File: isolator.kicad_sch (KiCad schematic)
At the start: 6 parts, among them U1 ADuM4165, U2 NUP4202, U3 NUP4202, Y1 24M

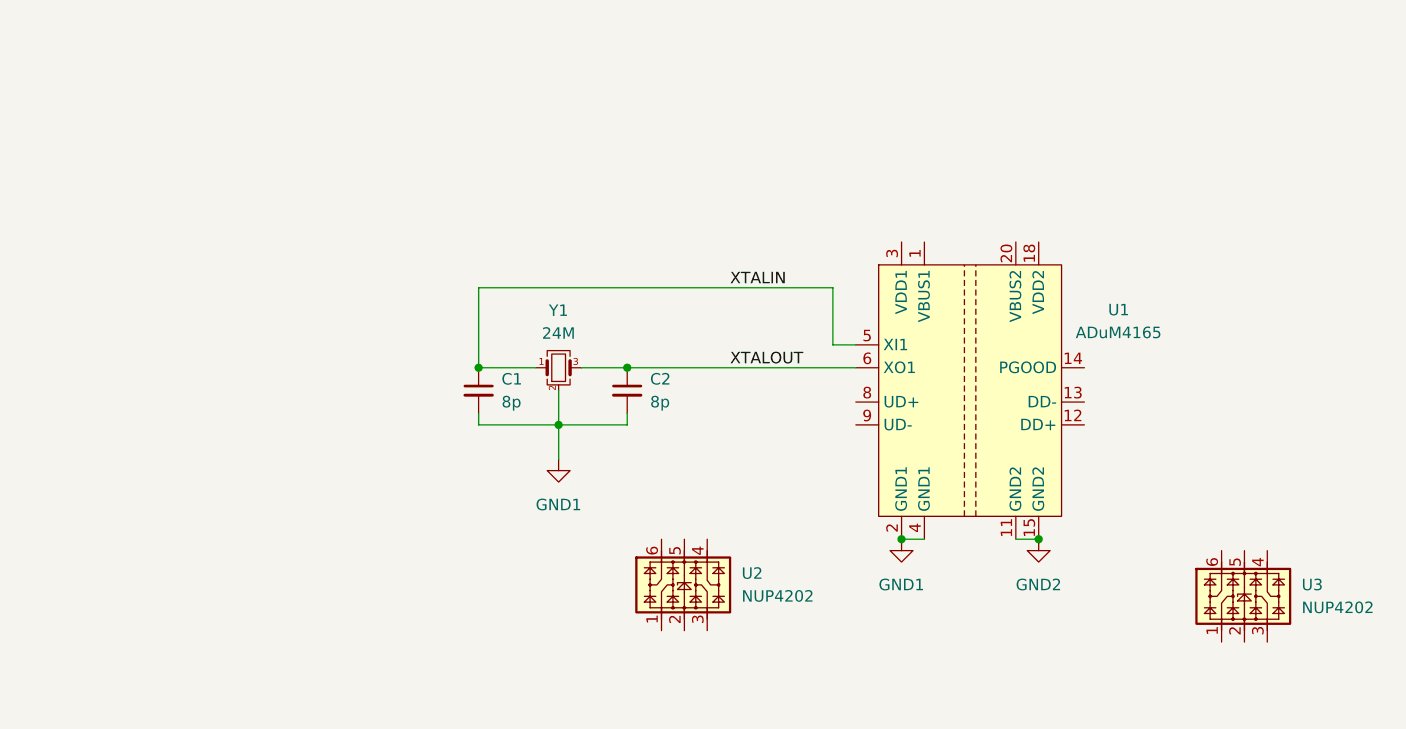
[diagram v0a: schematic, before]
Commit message: feat(sch): upstream USB-C host section
Add J1 (USB-C receptacle), R1/R2 (CC pull-downs), C3-C5 (VBUS_HOST/VDD1
decoupling) and wire VBUS_HOST, HOST_DP, HOST_DM, GND1 per the task-4
brief. Rewire U2 (NUP4202) as the host-side ESD array: two of its four
I/O channels clamp HOST_DP/HOST_DM, its GND pin ties to GND1, its VBUS
pin ties to VBUS_HOST, and the two unused channels get no_connect.
Terminate all ADuM4165 (U1) Side-1 pins; Side-2 pins not yet used by
this task get explicit no_connect markers.

Also add PWR_FLAG symbols on GND1, GND2, VBUS_HOST and VDD1, and
no_connect markers on U3's six pins, so `kicad-cli sch erc` exits 0
across the whole file (the project's ERC config marks
power_pin_not_driven as an error, and U3/GND2 were already unwired
pre-existing state) — flagged in the task report for whoever wires
U3/GND2 downstream.

Co-Authored-By: Claude Fable 5 <noreply@anthropic.com>
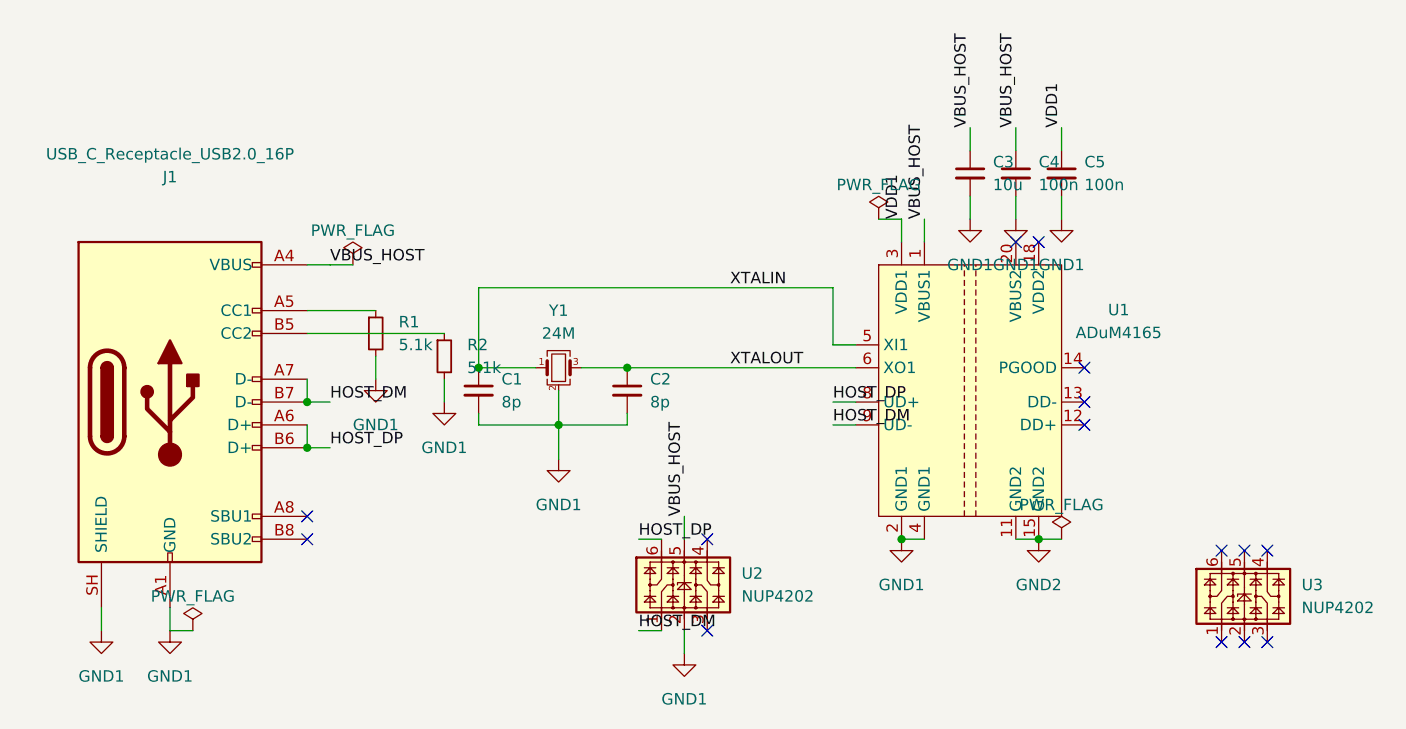
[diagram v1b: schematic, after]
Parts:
- added C3: 10u, symbol Device:C_Small
- added C4, C5: 100n, symbol Device:C_Small
- added J1: USB_C_Receptacle_USB2.0_16P, symbol Connector:USB_C_Receptacle_USB2.0_16P
- added R1, R2: 5.1k, symbol Device:R_Small
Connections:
- net GND1: now also U2.2, C3.2, C4.2, C5.2, J1.A1 (GND), J1.A12 (GND), J1.B1 (GND), J1.B12 (GND), J1.SH (SHIELD), R1.2, R2.2
- net HOST_DM: now reaches U2.1
- net HOST_DM: now also U1.9 (UD-), J1.A7 (D-), J1.B7 (D-)
- net VBUS_HOST: now reaches U2.5
- net VBUS_HOST: now also U1.1 (VBUS1), C3.1, C4.1, J1.A4 (VBUS), J1.A9 (VBUS), J1.B4 (VBUS), J1.B9 (VBUS)
- net HOST_DP: now reaches U2.6
- net HOST_DP: now also U1.8 (UD+), J1.A6 (D+), J1.B6 (D+)
- net VDD1: now reaches U1.3 (VDD1)
- net VDD1: now also C5.1
- new net: J1.A5 (CC1), R1.1
- new net: J1.B5 (CC2), R2.1
- no-connect marks 0 -> 15

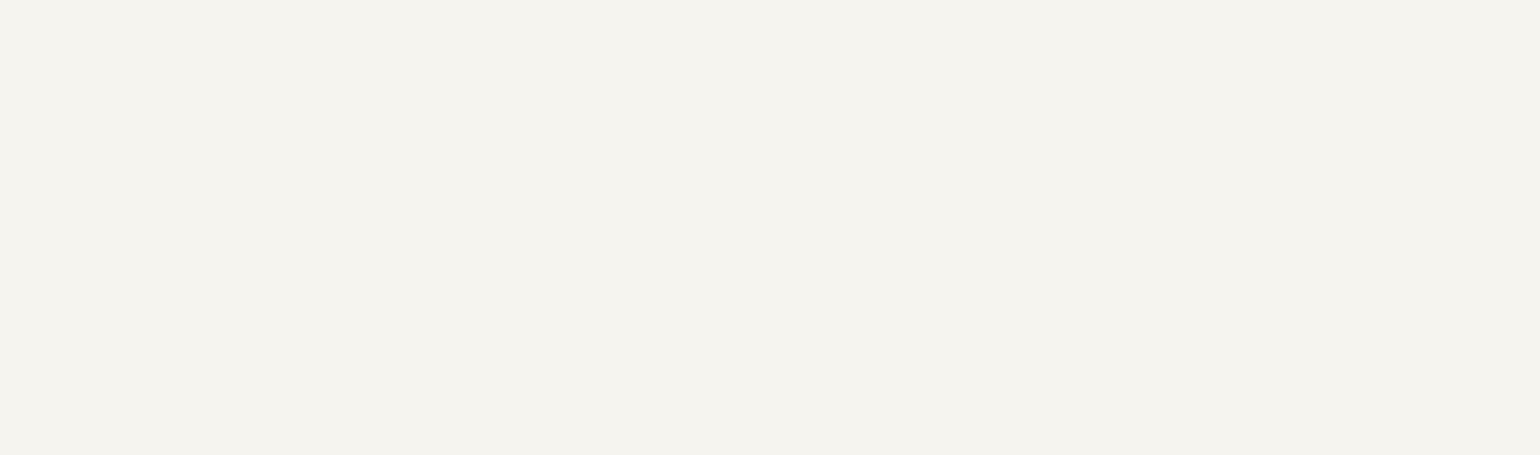
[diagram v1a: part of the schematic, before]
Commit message: feat(sch): SN6505B isolated DC-DC, 5V LDO
Add SN6505BDBV push-pull driver, WE-PPTI transformer (T1), full-wave
center-tap Schottky rectifier (D1/D2), and MIC29302WU adjustable LDO
(U6) implementing the bus-powered isolated DC-DC path: VBUS_HOST ->
U5/T1 -> DCDC_RAW (rectified, PWR_FLAG'd) -> U6 -> DCDC_5V (~4.97V via
30.1k/10k divider, Vref=1.24V confirmed against MIC29302WU datasheet).
T1 is the only component spanning the GND1/GND2 domains, per the
verified center-tapped-secondary topology from Task 2's extraction
(with a drive-by fix to that extraction's misstated isolation-test
pin numbers). kicad-cli sch erc --severity-error exits 0; analyzer net
membership matches spec exactly for DCDC_RAW, DCDC_5V, and the ADJ
feedback node, with no GND1/GND2 domain mixing.

Co-Authored-By: Claude Fable 5 <noreply@anthropic.com>
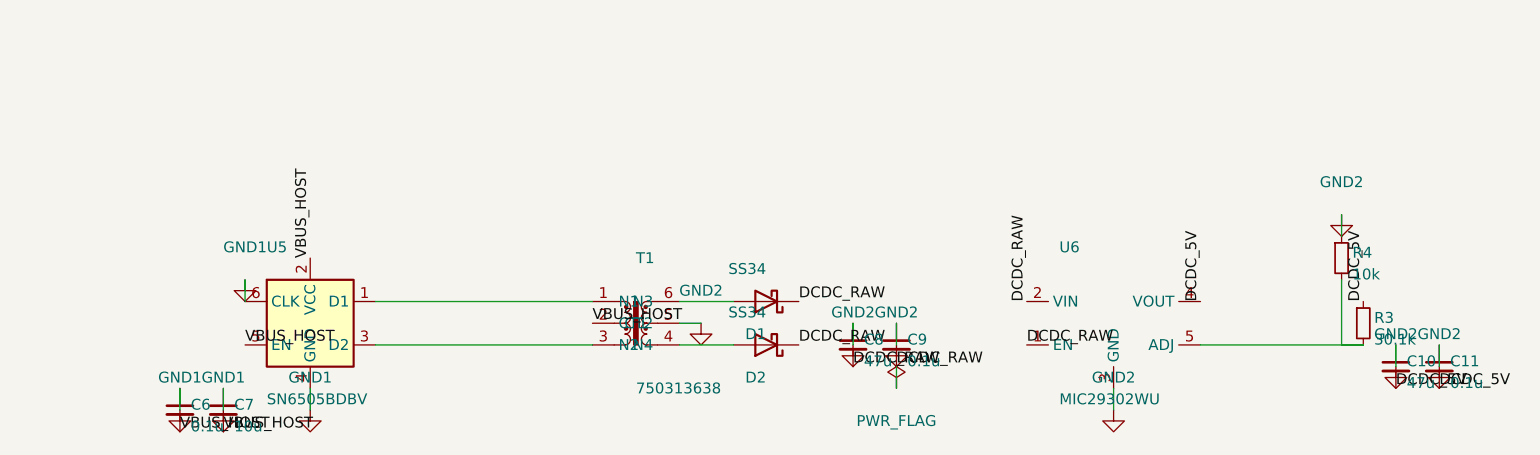
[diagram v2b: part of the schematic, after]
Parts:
- added C10, C8: 47u, symbol Device:C_Small
- added C11, C6, C9: 0.1u, symbol Device:C_Small
- added C7: 10u, symbol Device:C_Small
- added D1, D2: SS34, symbol Device:D_Schottky
- added R3: 30.1k, symbol Device:R_Small
- added R4: 10k, symbol Device:R_Small
- added T1: 750313638, symbol isolator-lib:750313638
- added U5: SN6505BDBV, Package_TO_SOT_SMD:SOT-23-6, symbol Power_Management:SN6505BDBV
- added U6: MIC29302WU, Package_TO_SOT_SMD:TO-263-5_TabPin3, symbol Regulator_Linear:MIC29302WU
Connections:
- net GND1: now also C6.1, C7.1, U5.4 (GND), U5.6 (CLK)
- net GND2: now also C10.1, C11.1, C8.1, C9.1, R4.1, T1.5 (CT2), U6.3 (GND)
- net VBUS_HOST: now also C6.2, C7.2, T1.2 (CT1), U5.2 (VCC), U5.5 (EN)
- new net: R3.2, R4.2, U6.5 (ADJ)
- new net: D2.2 (A), T1.4 (N4)
- new net: D1.2 (A), T1.6 (N3)
- new net: T1.1 (N1), U5.1 (D1)
- new net: T1.3 (N2), U5.3 (D2)
- new net DCDC_5V: C10.2, C11.2, R3.1, U6.4 (VOUT)
- new net DCDC_RAW: C8.2, C9.2, D1.1 (K), D2.1 (K), U6.1 (EN), U6.2 (VIN)

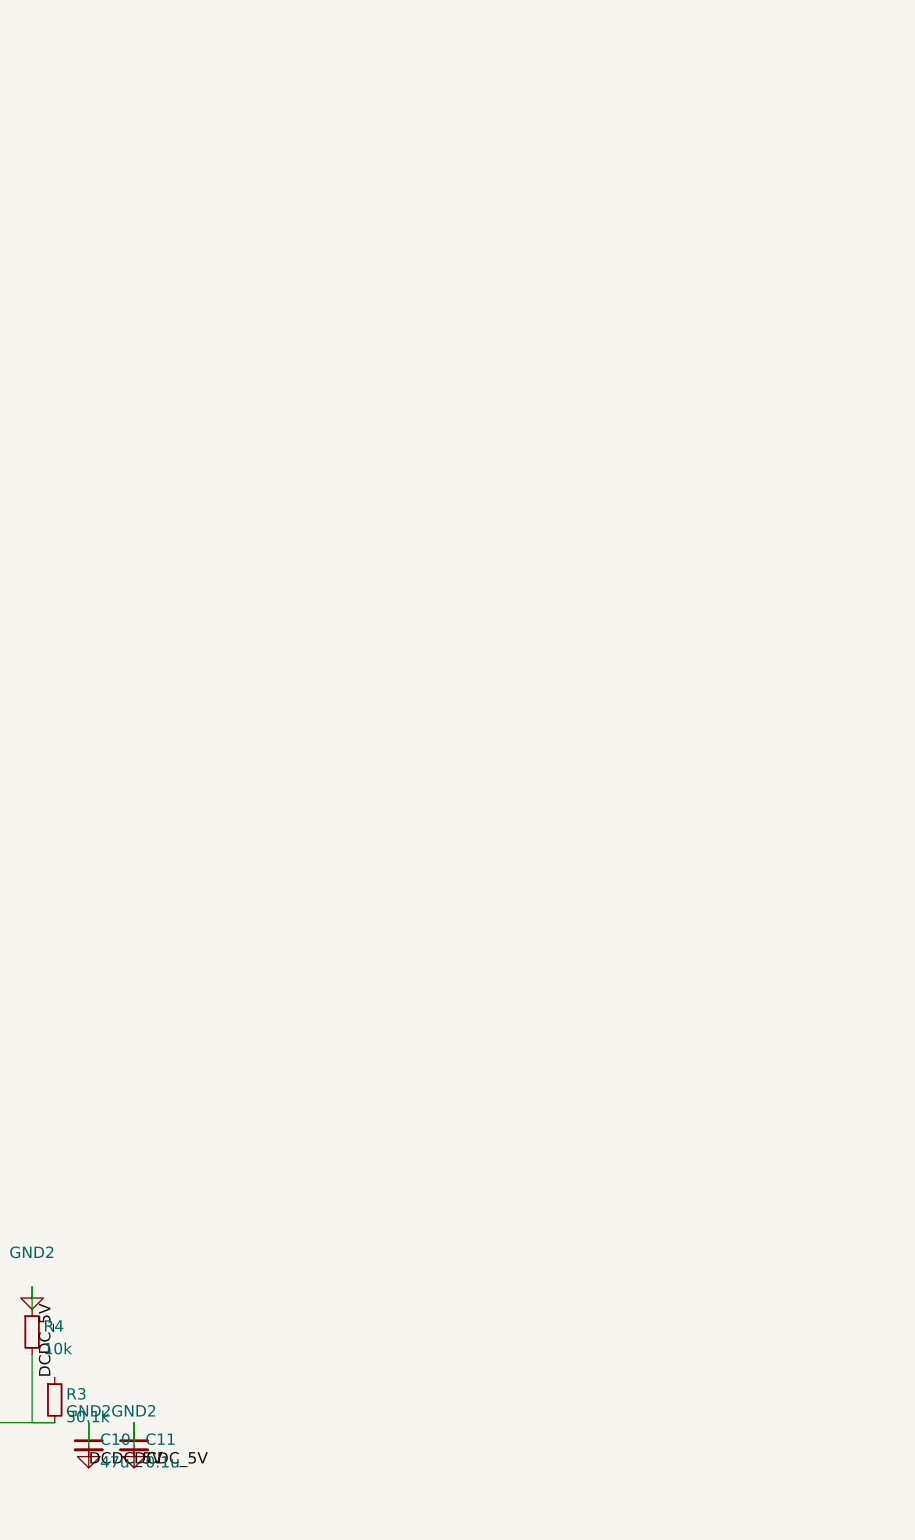
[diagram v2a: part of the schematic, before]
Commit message: feat(sch): external USB-C power, CC 3A detect, TPS2121 mux
Co-Authored-By: Claude Fable 5 <noreply@anthropic.com>
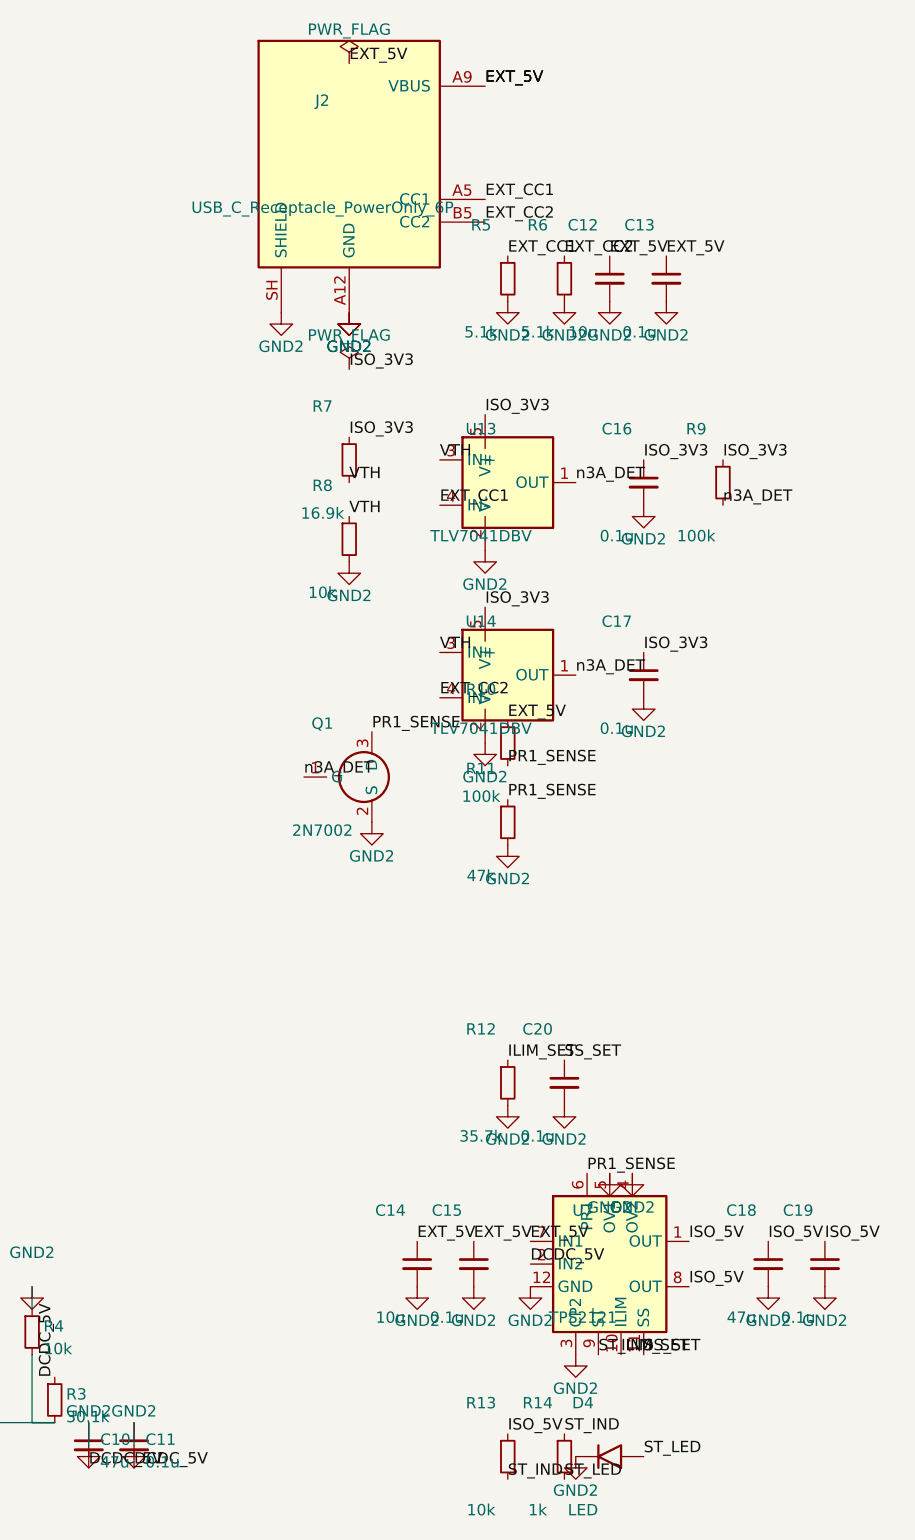
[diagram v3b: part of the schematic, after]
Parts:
- added C12, C14: 10u, symbol Device:C_Small
- added C13, C15, C16, C17, C19, C20: 0.1u, symbol Device:C_Small
- added C18: 47u, symbol Device:C_Small
- added D4: LED, symbol Device:LED
- added J2: USB_C_Receptacle_PowerOnly_6P, symbol Connector:USB_C_Receptacle_PowerOnly_6P
- added Q1: 2N7002, Package_TO_SOT_SMD:SOT-23, symbol Transistor_FET:2N7002
- added R10, R9: 100k, symbol Device:R_Small
- added R11: 47k, symbol Device:R_Small
- added R12: 35.7k, symbol Device:R_Small
- added R13, R8: 10k, symbol Device:R_Small
- added R14: 1k, symbol Device:R_Small
- added R5, R6: 5.1k, symbol Device:R_Small
- added R7: 16.9k, symbol Device:R_Small
- added U13, U14: TLV7041DBV, Package_TO_SOT_SMD:SOT-23-5, symbol Comparator:TLV7041DBV
- added U7: TPS2121, symbol isolator-lib:TPS2121
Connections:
- net DCDC_5V: now also U7.2 (IN2)
- net GND2: now also C12.2, C13.2, C14.2, C15.2, C16.2, C17.2, C18.2, C19.2, C20.2, D4.1 (K), J2.A12 (GND), J2.B12 (GND), J2.SH (SHIELD), Q1.2 (S), R11.2, R12.2, R5.2, R6.2, R8.2, U13.2 (V-), U14.2 (V-), U7.12 (GND), U7.3 (CP2), U7.4 (OV2), U7.5 (OV1)
- new net EXT_5V: C12.1, C13.1, C14.1, C15.1, J2.A9 (VBUS), J2.B9 (VBUS), R10.1, U7.7 (IN1)
- new net EXT_CC1: J2.A5 (CC1), R5.1, U13.4 (IN-)
- new net EXT_CC2: J2.B5 (CC2), R6.1, U14.4 (IN-)
- new net ILIM_SET: R12.1, U7.10 (ILIM)
- new net ISO_3V3: C16.1, C17.1, R7.1, R9.1, U13.5 (V+), U14.5 (V+)
- new net ISO_5V: C18.1, C19.1, R13.1, U7.1 (OUT), U7.8 (OUT)
- new net PR1_SENSE: Q1.3 (D), R10.2, R11.1, U7.6 (PR1)
- new net SS_SET: C20.1, U7.11 (SS)
- new net ST_IND: R13.2, R14.1, U7.9 (ST)
- new net ST_LED: D4.2 (A), R14.2
- new net VTH: R7.2, R8.1, U13.3 (IN+), U14.3 (IN+)
- new net n3A_DET: Q1.1 (G), R9.2, U13.1 (OUT), U14.1 (OUT)
